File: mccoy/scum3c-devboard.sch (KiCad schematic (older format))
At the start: 34 parts, among them J1 Conn_02x10_Odd_Even, J2 Conn_02x10_Odd_Even, J3 Conn_02x05_Odd_Even, J4 Conn_01x01_Male, U2 S-85S1AB18-I6T1U, U3 S-85S1AB11-I6T1U, U9AB1 ICM-20948

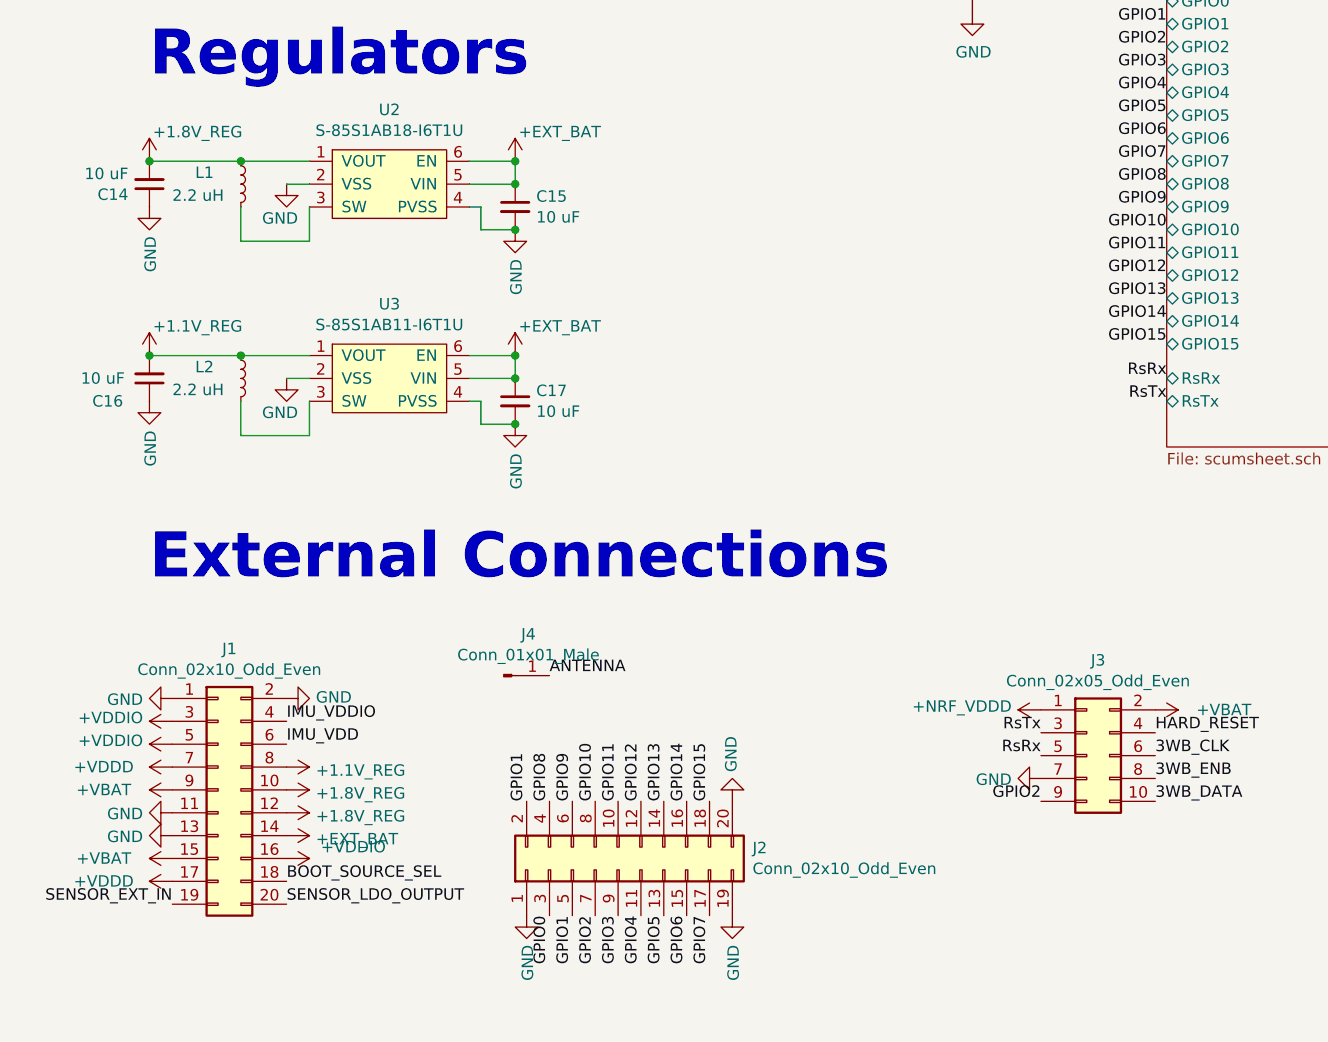
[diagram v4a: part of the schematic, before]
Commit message: routed regulator traces
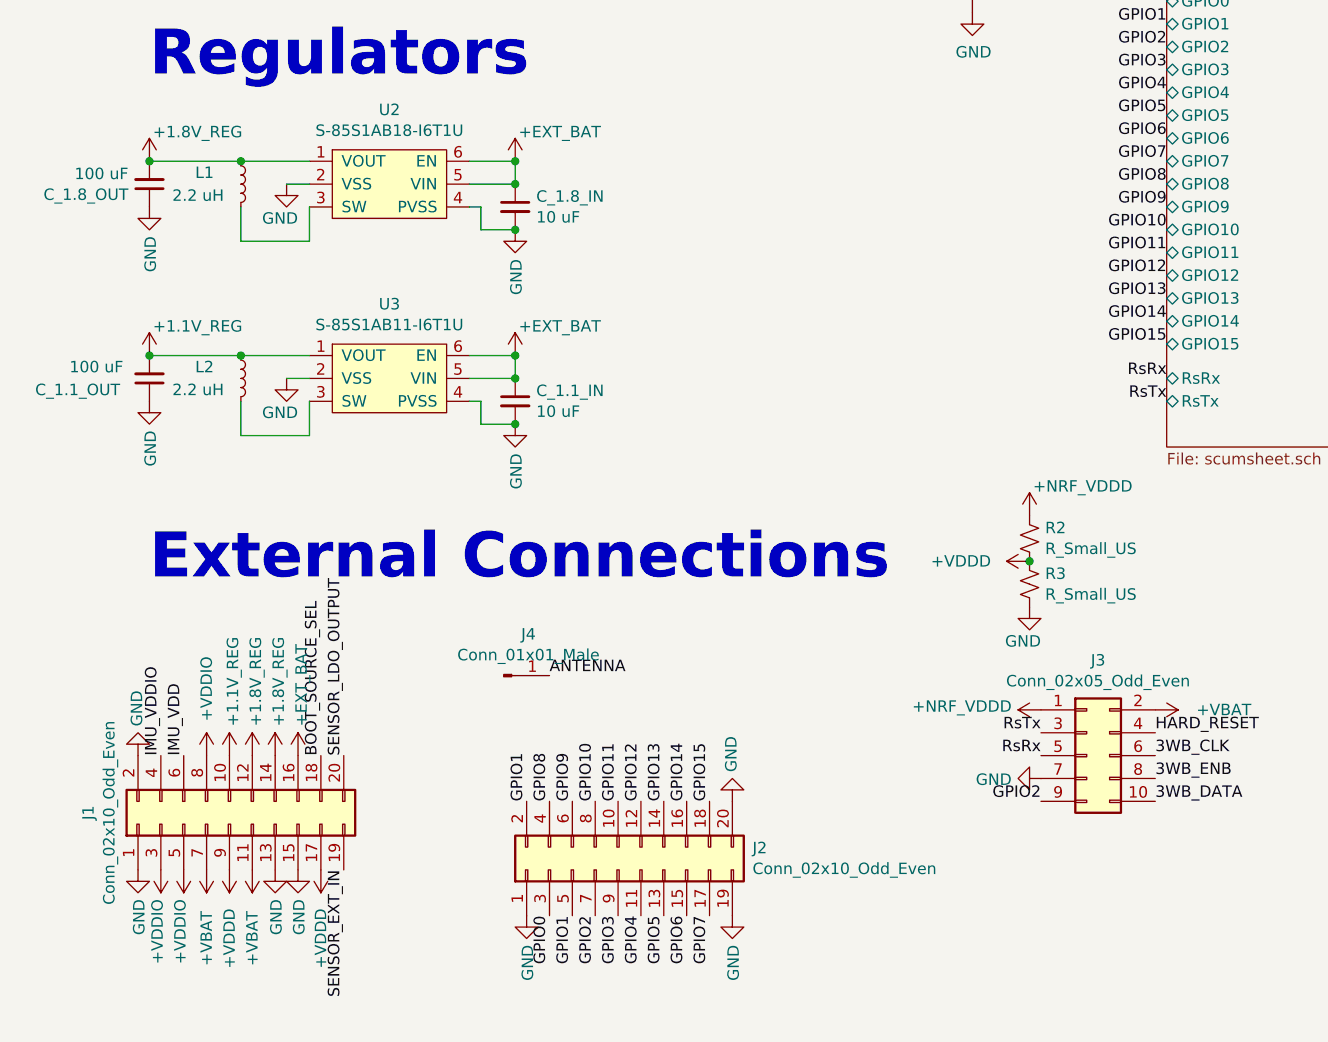
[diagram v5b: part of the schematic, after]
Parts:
- added R2, R3: R_Small_US, Resistor_SMD:R_0402_1005Metric, symbol Device:R_Small_US
- C_1.1_OUT: renamed from C16; value 10 uF -> 100 uF; footprint Capacitor_SMD:C_0402_1005Metric -> Capacitor_SMD:C_0805_2012Metric
- C_1.8_OUT: renamed from C14; value 10 uF -> 100 uF; footprint Capacitor_SMD:C_0402_1005Metric -> Capacitor_SMD:C_0805_2012Metric
- renumbered C17 to C_1.1_IN, C15 to C_1.8_IN
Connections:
- net +1.1V_REG: now also J1.10 (Pin_10); no longer J1.8 (Pin_8)
- net +1.8V_REG: now also J1.14 (Pin_14); no longer J1.10 (Pin_10)
- net +EXT_BAT: now also J1.16 (Pin_16); no longer J1.14 (Pin_14)
- net +NRF_VDDD: now also R2.1
- net +VBAT: now also J1.11 (Pin_11), J1.7 (Pin_7); no longer J1.15 (Pin_15), J1.9 (Pin_9)
- net +VDDD: now also J1.9 (Pin_9), R2.2, R3.1; no longer J1.7 (Pin_7)
- net +VDDIO: now also J1.8 (Pin_8); no longer J1.16 (Pin_16)
- net GND: now also J1.15 (Pin_15), R3.2; no longer J1.11 (Pin_11)
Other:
- moved on the sheet: J1

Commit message: numbered reg caps
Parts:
- renumbered C_1.1_IN to C_1.1_IN1, C_1.1_OUT to C_1.1_OUT1, C_1.8_IN to C_1.8_IN1, C_1.8_OUT to C_1.8_OUT1
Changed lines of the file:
@@
 $EndComp
 $Comp
-L Device:C_Small C_1.8_OUT
+L Device:C_Small C_1.8_OUT1
 U 1 1 612968B6
 P 1050 4450
-F 0 "C_1.8_OUT" H 1142 4496 50  0000 L CNN
+F 0 "C_1.8_OUT1" H 1142 4496 50  0000 L CNN
 F 1 "100 uF" H 1142 4405 50  0000 L CNN
 F 2 "Capacitor_SMD:C_0805_2012Metric" H 1050 4450 50  0001 C CNN
@@
 $EndComp
 $Comp
-L Device:C_Small C_1.1_OUT
+L Device:C_Small C_1.1_OUT1
 U 1 1 612ACBE1
 P 1050 5300
-F 0 "C_1.1_OUT" H 1550 5350 50  0000 R CNN
+F 0 "C_1.1_OUT1" H 1550 5350 50  0000 R CNN
 F 1 "100 uF" H 1400 5250 50  0000 R CNN
 F 2 "Capacitor_SMD:C_0805_2012Metric" H 1050 5300 50  0001 C CNN
@@
 $EndComp
 $Comp
-L Device:C_Small C_1.1_IN
+L Device:C_Small C_1.1_IN1
 U 1 1 612ACBED
 P 2650 5400
-F 0 "C_1.1_IN" H 2742 5446 50  0000 L CNN
+F 0 "C_1.1_IN1" H 2742 5446 50  0000 L CNN
 F 1 "10 uF" H 2742 5355 50  0000 L CNN
 F 2 "Capacitor_SMD:C_0402_1005Metric" H 2650 5400 50  0001 C CNN
@@
 $EndComp
 Connection ~ 2650 4350
-$Comp
-L Device:C_Small C_1.8_IN
-U 1 1 612980CF
-P 2650 4550
-F 0 "C_1.8_IN" H 2742 4596 50  0000 L CNN
-F 1 "10 uF" H 2742 4505 50  0000 L CNN
-F 2 "Capacitor_SMD:C_0402_1005Metric" H 2650 4550 50  0001 C CNN
-F 3 "~" H 2650 4550 50  0001 C CNN
-	1    2650 4550
-	1    0    0    -1
-$EndComp
 $Comp
 L Device:Battery_Cell BT1
@@
 	1    0    0    -1
 $EndComp
+$Comp
+L Device:C_Small C_1.8_IN1
+U 1 1 612980CF
+P 2650 4550
+F 0 "C_1.8_IN1" H 2742 4596 50  0000 L CNN
+F 1 "10 uF" H 2742 4505 50  0000 L CNN
+F 2 "Capacitor_SMD:C_0402_1005Metric" H 2650 4550 50  0001 C CNN
+F 3 "~" H 2650 4550 50  0001 C CNN
+	1    2650 4550
+	1    0    0    -1
+$EndComp

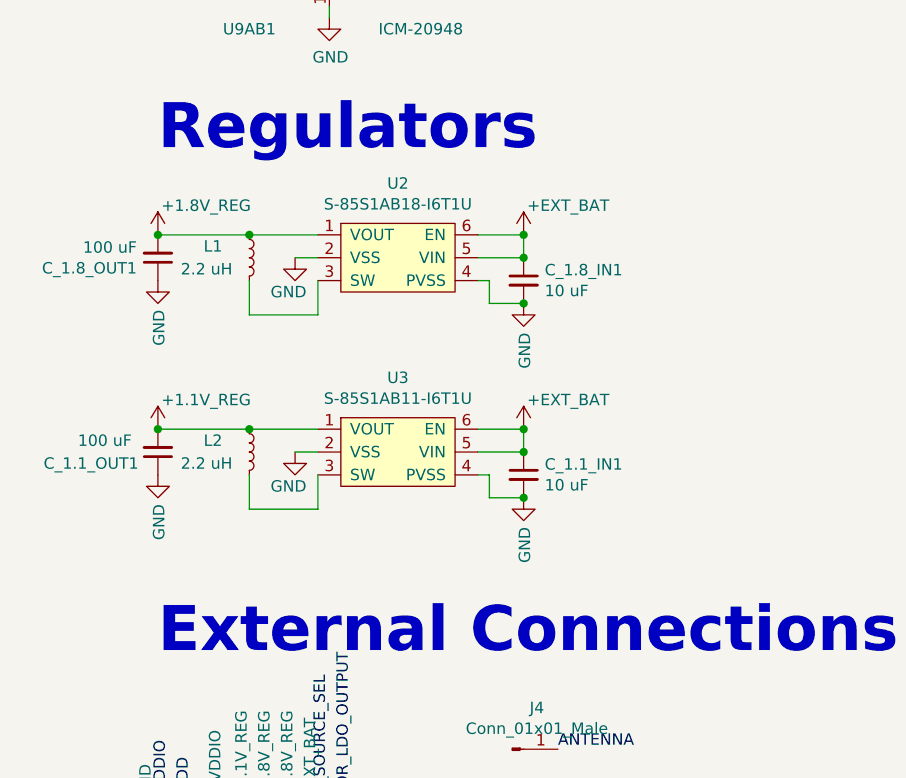
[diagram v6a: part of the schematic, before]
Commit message: changed regulators to copy-pasted from spock
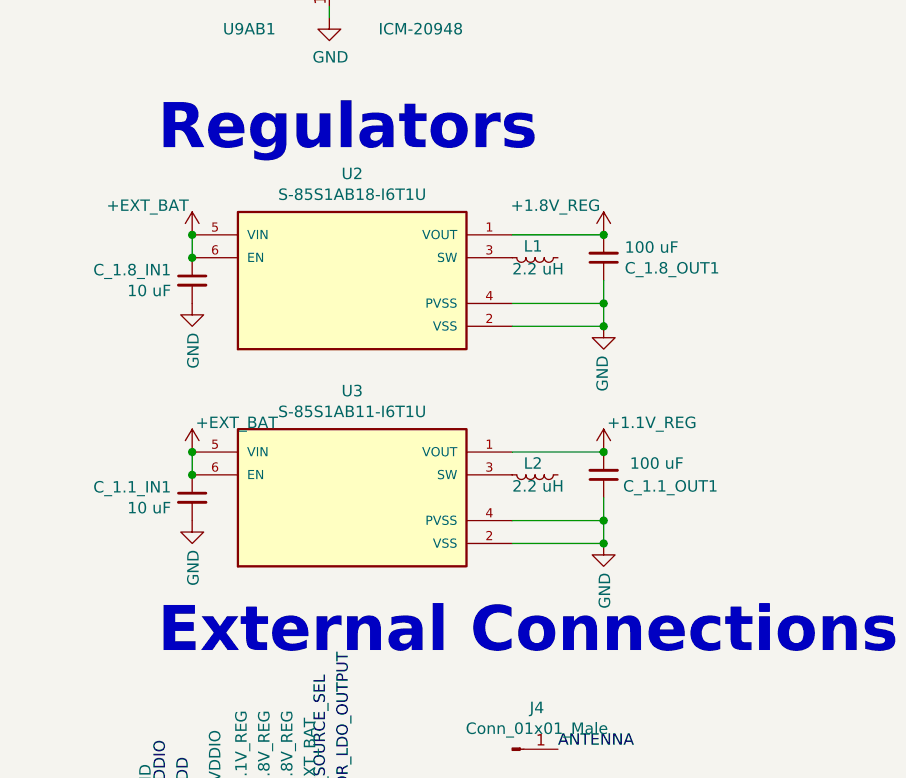
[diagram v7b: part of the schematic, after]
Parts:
- removed U2: S-85S1AB18-I6T1U, SCUM:SNT-6A, symbol draft1library:S-85S1AB18-I6T1U
- removed U3: S-85S1AB11-I6T1U, SCUM:SNT-6A, symbol draft1library:S-85S1AB11-I6T1U
- added U2: S-85S1AB18-I6T1U, downloaded_libs:SOFL50P180X50-6N, symbol S-85S1AB20-I6T1U:S-85S1AB18-I6T1U
- added U3: S-85S1AB11-I6T1U, downloaded_libs:SOFL50P180X50-6N, symbol S-85S1AB20-I6T1U:S-85S1AB11-I6T1U
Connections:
- net +1.1V_REG: now also U3.1 (VOUT); no longer L2.1
- net +1.8V_REG: now also U2.1 (VOUT); no longer L1.1
- net +EXT_BAT: now also U2.5 (VIN), U2.6 (EN), U3.5 (VIN), U3.6 (EN)
- net GND: now also U2.2 (VSS), U2.4 (PVSS), U3.2 (VSS), U3.4 (PVSS)
- net at L2.2: now also U3.3 (SW)
- net at L1.2: now also U2.3 (SW)
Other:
- moved on the sheet: C_1.1_IN1, C_1.1_OUT1, C_1.8_IN1, C_1.8_OUT1, L1, L2

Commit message: started adding labels
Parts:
- removed BT1: Battery_Cell, Battery:Battery_Panasonic_CR2032-VS1N_Vertical_CircularHoles, symbol Device:Battery_Cell
- added BT1: BK-870, downloaded_libs:MPD_BK-870, symbol BK-870:BK-870
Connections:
- net +1.1V_REG: now also L2.1
- net +1.8V_REG: now also L1.1
- net +EXT_BAT: now also BT1.1, BT1.3
- net GND: now also BT1.2
- net IMU_VDD: now also J1.4 (Pin_4); no longer J1.6 (Pin_6)
- net IMU_VDDIO: now also J1.6 (Pin_6); no longer J1.4 (Pin_4)
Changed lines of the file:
@@
 Text Label 1700 1750 2    50   ~ 0
 IMU_VDDIO
-Text Label 1100 6950 1    50   ~ 0
+Text Label 1200 6950 1    50   ~ 0
 IMU_VDDIO
 Text Label 3200 7150 1    50   ~ 0
@@
 Text Label 3500 7150 1    50   ~ 0
 GPIO15
-Text Label 1200 6950 1    50   ~ 0
+Text Label 1100 6950 1    50   ~ 0
 IMU_VDD
 NoConn ~ 1300 2950
@@
 $EndSheet
 $Comp
-L draft1library:+VBAT #PWR048
-U 1 1 608BF8E8
-P 9850 1650
-F 0 "#PWR048" H 9850 1500 50  0001 C CNN
-F 1 "+VBAT" H 9865 1823 50  0000 C CNN
-F 2 "" H 9850 1650 50  0001 C CNN
-F 3 "" H 9850 1650 50  0001 C CNN
-	1    9850 1650
-	1    0    0    -1
-$EndComp
-$Comp
-L power:GND #PWR046
-U 1 1 608BFCDC
-P 9850 2000
-AR Path="/608BFCDC" Ref="#PWR046"  Part="1"
-AR Path="/5F3B0B28/608BFCDC" Ref="#PWR?"  Part="1"
-F 0 "#PWR046" H 9850 1750 50  0001 C CNN
-F 1 "GND" H 9855 1827 50  0000 C CNN
-F 2 "" H 9850 2000 50  0001 C CNN
-F 3 "" H 9850 2000 50  0001 C CNN
-	1    9850 2000
-	1    0    0    -1
-$EndComp
-$Comp
 L draft1library:+VDDIO #PWR?
 U 1 1 60873674
@@
 $EndComp
 Connection ~ 1200 4350
-$Comp
-L Device:Battery_Cell BT1
-U 1 1 612886A9
-P 9850 1850
-F 0 "BT1" H 9968 1946 50  0000 L CNN
-F 1 "Battery_Cell" H 9968 1855 50  0000 L CNN
-F 2 "Battery:Battery_Panasonic_CR2032-VS1N_Vertical_CircularHoles" V 9850 1910 50  0001 C CNN
-F 3 "~" V 9850 1910 50  0001 C CNN
-	1    9850 1850
-	1    0    0    -1
-$EndComp
 Text Notes 1050 4000 0    197  ~ 39
 Regulators
@@
 $EndComp
 Wire Wire Line
-	3000 4350 2600 4350
+	3000 4350 2800 4350
 Wire Wire Line
 	2600 4750 3000 4750
@@
 Connection ~ 3000 4650
 Wire Wire Line
-	2600 5300 3000 5300
+	2600 5300 2800 5300
 Wire Wire Line
 	1200 5300 1200 5400
@@
 	2600 5700 3000 5700
 Connection ~ 3000 5700
+$Comp
+L BK-870:BK-870 BT1
+U 1 1 61426DB6
+P 10000 2600
+F 0 "BT1" V 9954 2730 50  0000 L CNN
+F 1 "BK-870" V 10045 2730 50  0000 L CNN
+F 2 "downloaded_libs:MPD_BK-870" H 10000 2600 50  0001 L BNN
+F 3 "" H 10000 2600 50  0001 L BNN
+F 4 "D" H 10000 2600 50  0001 L BNN "PARTREV"
+F 5 "MPD" H 10000 2600 50  0001 L BNN "MANUFACTURER"
+F 6 "Manufacturer Recommendation" H 10000 2600 50  0001 L BNN "STANDARD"
+	1    10000 2600
+	0    1    1    0
+$EndComp
+$Comp
+L power:GND #PWR046
+U 1 1 608BFCDC
+P 10000 2800
+AR Path="/608BFCDC" Ref="#PWR046"  Part="1"
+AR Path="/5F3B0B28/608BFCDC" Ref="#PWR?"  Part="1"
+F 0 "#PWR046" H 10000 2550 50  0001 C CNN
+F 1 "GND" H 10005 2627 50  0000 C CNN
+F 2 "" H 10000 2800 50  0001 C CNN
+F 3 "" H 10000 2800 50  0001 C CNN
+	1    10000 2800
+	1    0    0    -1
+$EndComp
+Wire Wire Line
+	2800 5400 2800 5300
+Connection ~ 2800 5300
+Wire Wire Line
+	2800 5300 3000 5300
+Wire Wire Line
+	2800 4450 2800 4350
+Connection ~ 2800 4350
+Wire Wire Line
+	2800 4350 2600 4350
+$Comp
+L draft1library:+EXT_BAT #PWR?
+U 1 1 6148DC5B
+P 10000 2400
+F 0 "#PWR?" H 10000 2250 50  0001 C CNN
+F 1 "+EXT_BAT" H 10015 2528 50  0000 L CNN
+F 2 "" H 10000 2400 50  0001 C CNN
+F 3 "" H 10000 2400 50  0001 C CNN
+	1    10000 2400
+	-1   0    0    -1
+$EndComp
+$Comp
+L draft1library:+EXT_BAT #PWR?
+U 1 1 6148E3AA
+P 9150 1350
+F 0 "#PWR?" H 9150 1200 50  0001 C CNN
+F 1 "+EXT_BAT" H 9165 1478 50  0000 L CNN
+F 2 "" H 9150 1350 50  0001 C CNN
+F 3 "" H 9150 1350 50  0001 C CNN
+	1    9150 1350
+	1    0    0    1
+$EndComp
+$Comp
+L power:PWR_FLAG #FLG?
+U 1 1 6148F1C6
+P 9150 1350
+AR Path="/6148F1C6" Ref="#FLG?"  Part="1"
+AR Path="/5F3B0B28/6148F1C6" Ref="#FLG?"  Part="1"
+F 0 "#FLG?" H 9150 1425 50  0001 C CNN
+F 1 "PWR_FLAG" H 9150 1523 50  0000 C CNN
+F 2 "" H 9150 1350 50  0001 C CNN
+F 3 "~" H 9150 1350 50  0001 C CNN
+	1    9150 1350
+	1    0    0    -1
+$EndComp
 $EndSCHEMATC
